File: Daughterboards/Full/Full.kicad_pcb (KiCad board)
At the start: 2 copper layers, 76.9 x 36 mm, 38 parts, among them J1 I2C EXT, J2 HRO-TYPEC-M12, J3 BATTERY JST, J4 USB_A, J5 USB_A, J6 FFC, M1 M.2_Key_E, U2 USB2514B_Bi, U3 XC6206P332MR, Y1 12MHZ

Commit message: connect the ffc to the m.2 on the full
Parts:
- added C12: 4.7uF, Capacitor_SMD:C_0402_1005Metric, F.Cu at (62.2, 12.9)
- added C13: 1uF, Capacitor_SMD:C_0402_1005Metric, F.Cu at (62.2, 11.9)
- added C14: 1uF, Capacitor_SMD:C_0402_1005Metric, F.Cu at (64.2, 7.40)
- added J7: Conn_01x05, Connector_PinSocket_2.54mm:PinSocket_2x03_P2.54mm_Vertical, F.Cu at (53.4, 8.01)
- added M1: M.2_Key_E, m2ngff:m2-bracket-key-e, F.Cu at (55.8, 23.9)
- added U4: XC6206P332MR, Package_TO_SOT_SMD:SOT-23, F.Cu at (63.2, 9.65)
- moved J3 0.25 mm to (18.6, 30.5)
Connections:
- J1 pad 2: I2C_SDA -> I2C_SCL
- J1 pad 3: I2C_SCL -> I2C_SDA
- J6 pad 1: unconnected-(J6-Pad1) -> I2C_SCL
- J6 pad 10: unconnected-(J6-Pad10) -> P2
- J6 pad 11: unconnected-(J6-Pad11) -> P3
- J6 pad 12: unconnected-(J6-Pad12) -> P4
- J6 pad 13: unconnected-(J6-Pad13) -> P5
- J6 pad 14: unconnected-(J6-Pad14) -> P6
- J6 pad 15: unconnected-(J6-Pad15) -> P27
- J6 pad 16: unconnected-(J6-Pad16) -> P26
- J6 pad 17: unconnected-(J6-Pad17) -> P25
- J6 pad 18: unconnected-(J6-Pad18) -> P24
- J6 pad 19: unconnected-(J6-Pad19) -> P23
- J6 pad 2: unconnected-(J6-Pad2) -> I2C_SDA
- J6 pad 20: unconnected-(J6-Pad20) -> P22
- J6 pad 21: unconnected-(J6-Pad21) -> P21
- J6 pad 22: unconnected-(J6-Pad22) -> P20
- J6 pad 23: unconnected-(J6-Pad23) -> P19
- J6 pad 24: unconnected-(J6-Pad24) -> P18
- J6 pad 25: unconnected-(J6-Pad25) -> P17
- J6 pad 26: unconnected-(J6-Pad26) -> P16
- J6 pad 27: unconnected-(J6-Pad27) -> P15
- J6 pad 28: unconnected-(J6-Pad28) -> P14
- J6 pad 29: +3V3 -> mbout
- J6 pad 3: unconnected-(J6-Pad3) -> P11
- J6 pad 4: unconnected-(J6-Pad4) -> P10
- J6 pad 5: unconnected-(J6-Pad5) -> P9
- J6 pad 6: unconnected-(J6-Pad6) -> P8
- J6 pad 7: unconnected-(J6-Pad7) -> P7
- J6 pad 8: unconnected-(J6-Pad8) -> P0
- J6 pad 9: unconnected-(J6-Pad9) -> P1
- M1 pad 10: unconnected-(M1-Pad10) -> vout
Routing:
- net I2C_SDA: track 0.00 -> 60.4 mm, vias 0 -> 2
- net I2C_SCL: track 0.00 -> 59.7 mm, vias 0 -> 2
- net P6: track 0.00 -> 23.1 mm, vias 0 -> 2
- net P5: track 0.00 -> 23.0 mm, vias 0 -> 2
- net P4: track 0.00 -> 22.9 mm, vias 0 -> 2
- net P3: track 0.00 -> 22.8 mm, vias 0 -> 2
- net P2: track 0.00 -> 22.7 mm, vias 0 -> 2
- net P0: track 0.00 -> 22.5 mm, vias 0 -> 2
- net P1: track 0.00 -> 22.5 mm, vias 0 -> 2
- net P11: track 0.00 -> 22.1 mm, vias 0 -> 2
- net P10: track 0.00 -> 21.5 mm, vias 0 -> 2
- net P9: track 0.00 -> 21.2 mm, vias 0 -> 2
- net P8: track 0.00 -> 20.9 mm, vias 0 -> 2
- net P7: track 0.00 -> 20.9 mm, vias 0 -> 2
- net P25: track 0.00 -> 18.3 mm
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
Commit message: finish the full db
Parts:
- removed the M1 at (55.8, 23.9)
- added LO3: MUD LOGO, LogoSmall:LogoSmall_Cu, B.Cu at (64.0, 31.9)
- added LO4: TapTap Logo, LogoSmall:tt_4mm, B.Cu at (69.3, 32.5)
- added Ref**: Val**, LogoSmall:Full-brd, F.Cu at (136.1, -100.8)
- added kibuzzard-623B2553: G***, kibuzzard-623B2553, B.Cu at (57.8, 14.0)
- added kibuzzard-623B2559: G***, kibuzzard-623B2559, B.Cu at (55.2, 14.0)
- added kibuzzard-623B2562: G***, kibuzzard-623B2562, B.Cu at (52.7, 14.0)
- added kibuzzard-623B2578: G***, kibuzzard-623B2578, B.Cu at (52.7, 4.49)
- added kibuzzard-623B2586: G***, kibuzzard-623B2586, B.Cu at (55.2, 4.48)
- J7: value Conn_01x05 -> Conn_02x03_Odd_Even
- LO2: value Puzzle Logo -> MUD LOGO; footprint LogoSmall:LogoSmall -> LogoSmall:LogoSmall_Cu
- moved LO1 22.0 mm to (69.5, 31.6)
- moved LO2 21.8 mm to (64.0, 31.4)
- moved M1 0.81 mm to (56.2, 24.6)
- moved H5 0.81 mm to (26.4, 24.6)
- moved J7 0.70 mm to (52.7, 8.01)
- moved C2 0.10 mm to (7.58, 13.1)
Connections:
- J7 pad 3: DEBUG1 -> GND
- J7 pad 6: (no net) -> DEBUG1
- LO2 pad 1: (no net) -> reset1
- LO2 pad 2: (no net) -> reset2
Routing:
- net reset2: track 9.75 -> 41.3 mm, vias 1 -> 3
- net reset1: track 9.05 -> 38.8 mm, vias 1 -> 2
- net GND: track 28.2 -> 47.7 mm, vias 11 -> 23
- net DEBUG1: track 22.5 -> 19.4 mm
- net DEBUG3: track 23.9 -> 26.4 mm
- net DEBUG2: track 21.5 -> 24.0 mm
- net P0: track 22.5 -> 21.7 mm
- net P1: track 22.5 -> 21.8 mm
- net P3: track 22.8 -> 22.1 mm
- net P6: track 23.1 -> 22.5 mm
- net P4: track 22.9 -> 22.2 mm
- net P2: track 22.7 -> 22.0 mm
- net P5: track 23.0 -> 22.4 mm
- net vout: track 16.9 -> 17.5 mm
- net P27: track 18.3 -> 18.8 mm
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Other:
- board text added: "MUD Daughterboard Full Edition M.2+Hub+I2C"

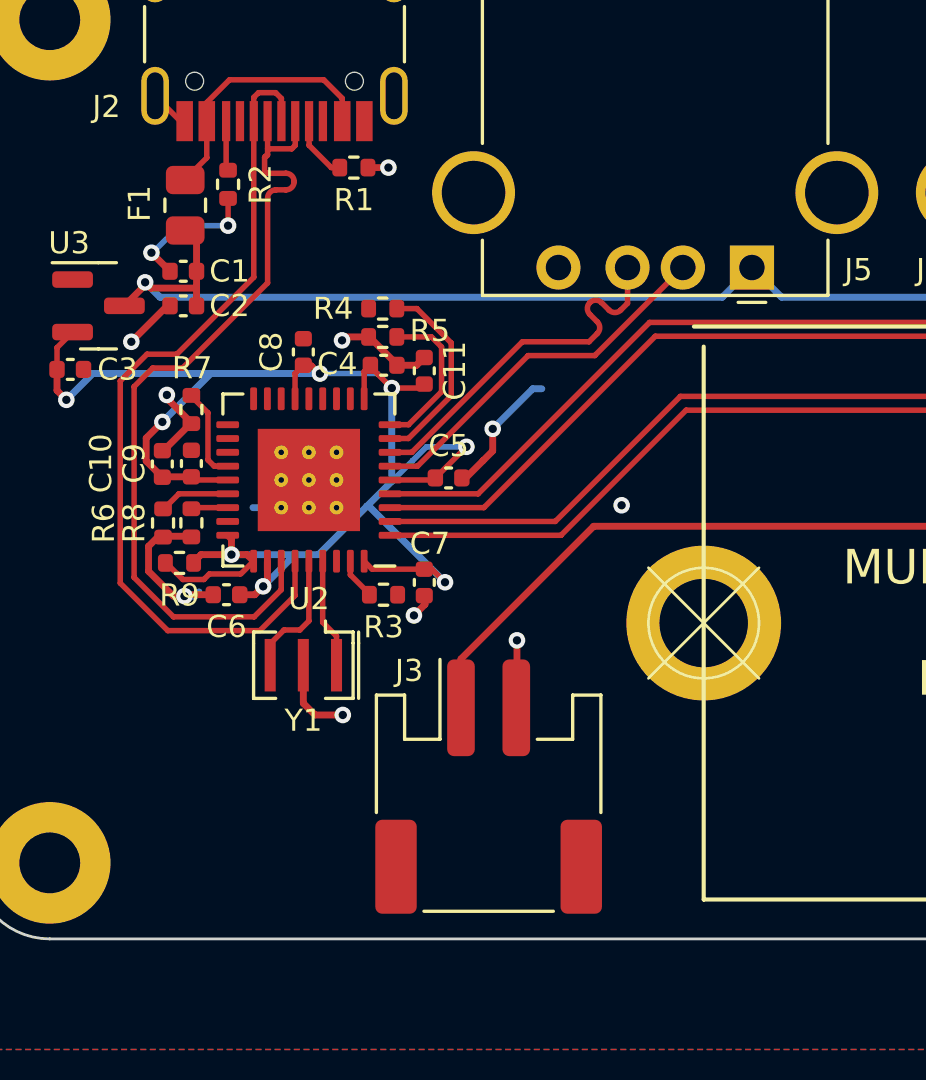
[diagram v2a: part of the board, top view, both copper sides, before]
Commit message: fix the puzzle back after i accidentally removed it
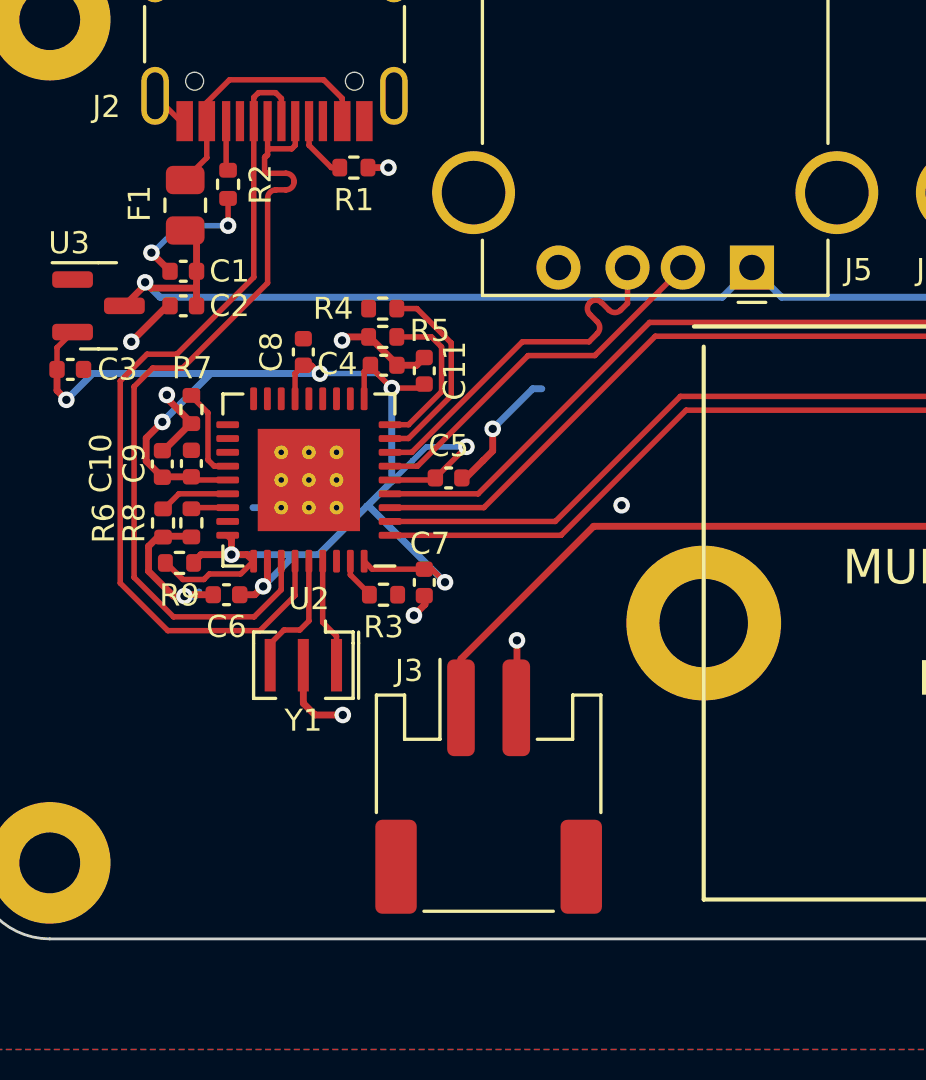
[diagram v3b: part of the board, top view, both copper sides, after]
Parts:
- moved Ref** 153.8 mm to (38.5, 18.0)

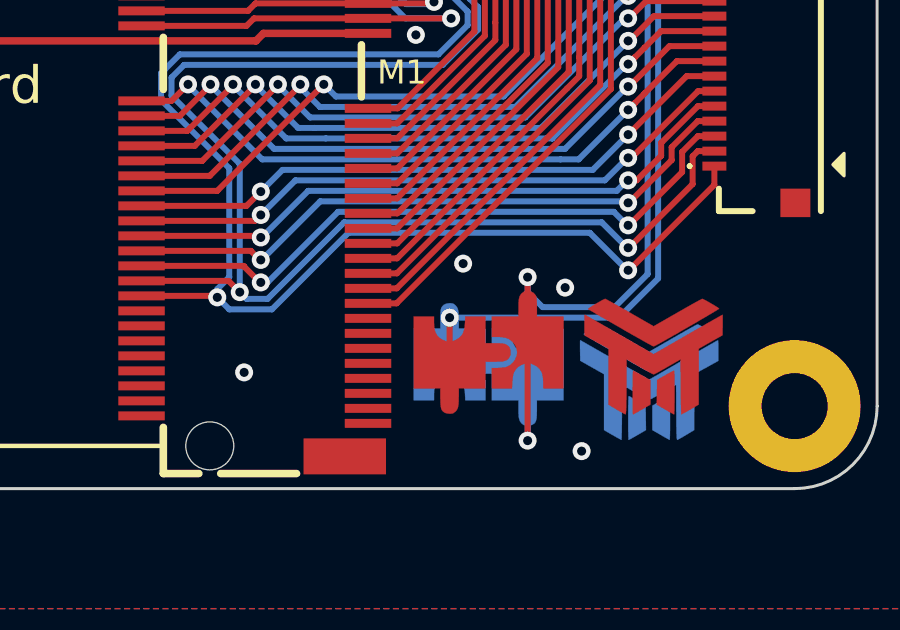
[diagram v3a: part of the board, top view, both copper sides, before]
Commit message: add soft symlink to point to the 3d for marbastlib links
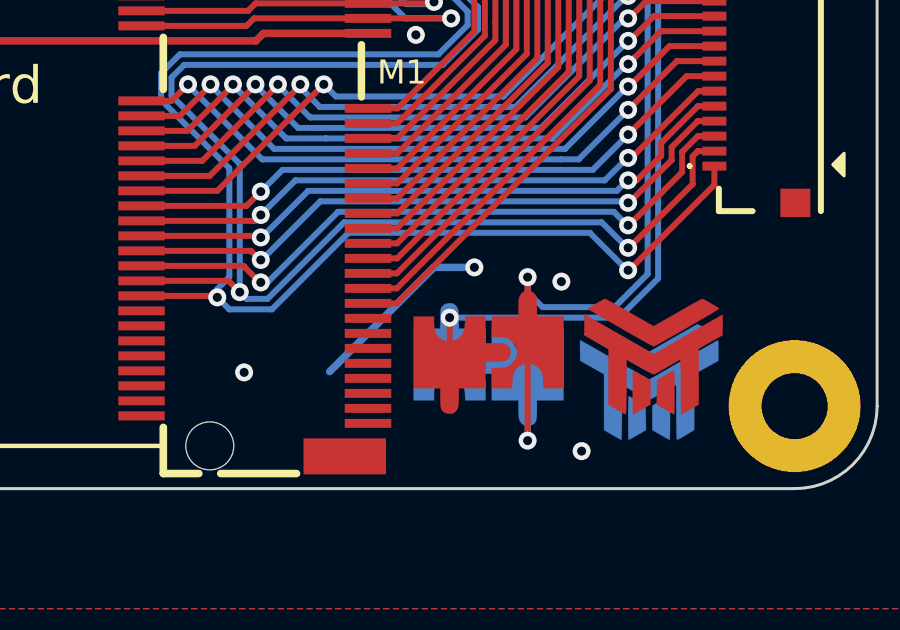
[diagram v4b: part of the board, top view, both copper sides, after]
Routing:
- net GND: track 47.7 -> 54.0 mm
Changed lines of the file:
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@@
   (via (at 9.2 10.2) (size 0.6) (drill 0.3) (layers "F.Cu" "B.Cu") (net 2))
   (via (at 6.986716 16.323517) (size 0.6) (drill 0.3) (layers "F.Cu" "B.Cu") (net 2))
-  (via (at 63.1 28.5) (size 0.6) (drill 0.3) (layers "F.Cu" "B.Cu") (free) (net 2))
+  (via (at 63.475 28.625) (size 0.6) (drill 0.3) (layers "F.Cu" "B.Cu") (free) (net 2))
   (via (at 15.922699 24.3) (size 0.6) (drill 0.3) (layers "F.Cu" "B.Cu") (net 2))
   (via (at 62.45 8.5) (size 0.6) (drill 0.3) (layers "F.Cu" "B.Cu") (net 2))
@@
   (via (at 7.622699 23.6) (size 0.6) (drill 0.3) (layers "F.Cu" "B.Cu") (net 2))
   (via (at 50.725 17.065) (size 0.6) (drill 0.3) (layers "F.Cu" "B.Cu") (net 2))
-  (via (at 66.5 29.3) (size 0.6) (drill 0.3) (layers "F.Cu" "B.Cu") (free) (net 2))
+  (via (at 66.375 29.1) (size 0.6) (drill 0.3) (layers "F.Cu" "B.Cu") (free) (net 2))
   (via (at 18.772699 17.55) (size 0.6) (drill 0.3) (layers "F.Cu" "B.Cu") (net 2))
   (via (at 13.35 27.9) (size 0.6) (drill 0.3) (layers "F.Cu" "B.Cu") (net 2))
@@
   (via (at 55.8 32.125) (size 0.6) (drill 0.3) (layers "F.Cu" "B.Cu") (free) (net 2))
   (via (at 61.225 16.4) (size 0.6) (drill 0.3) (layers "F.Cu" "B.Cu") (net 2))
+  (segment (start 62.125 28.625) (end 58.65 32.1) (width 0.25) (layer "B.Cu") (net 2))
   (segment (start 8 23.6) (end 8.15 23.45) (width 0.25) (layer "B.Cu") (net 2))
   (segment (start 9.2 10.2) (end 7.45 10.2) (width 0.2) (layer "B.Cu") (net 2))
   (segment (start 20.222699 16.1) (end 20.55 16.1) (width 0.25) (layer "B.Cu") (net 2))
+  (segment (start 63.475 28.625) (end 62.125 28.625) (width 0.25) (layer "B.Cu") (net 2))
   (segment (start 7.45 10.2) (end 6.471752 11.178248) (width 0.2) (layer "B.Cu") (net 2))
   (segment (start 18.772699 17.55) (end 20.222699 16.1) (width 0.25) (layer "B.Cu") (net 2))
